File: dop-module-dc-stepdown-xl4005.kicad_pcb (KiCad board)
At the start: 4 copper layers, 53.3 x 27.9 mm, 16 parts, among them J101 Conn_01x02, J102 Conn_01x02, U101 XL4005

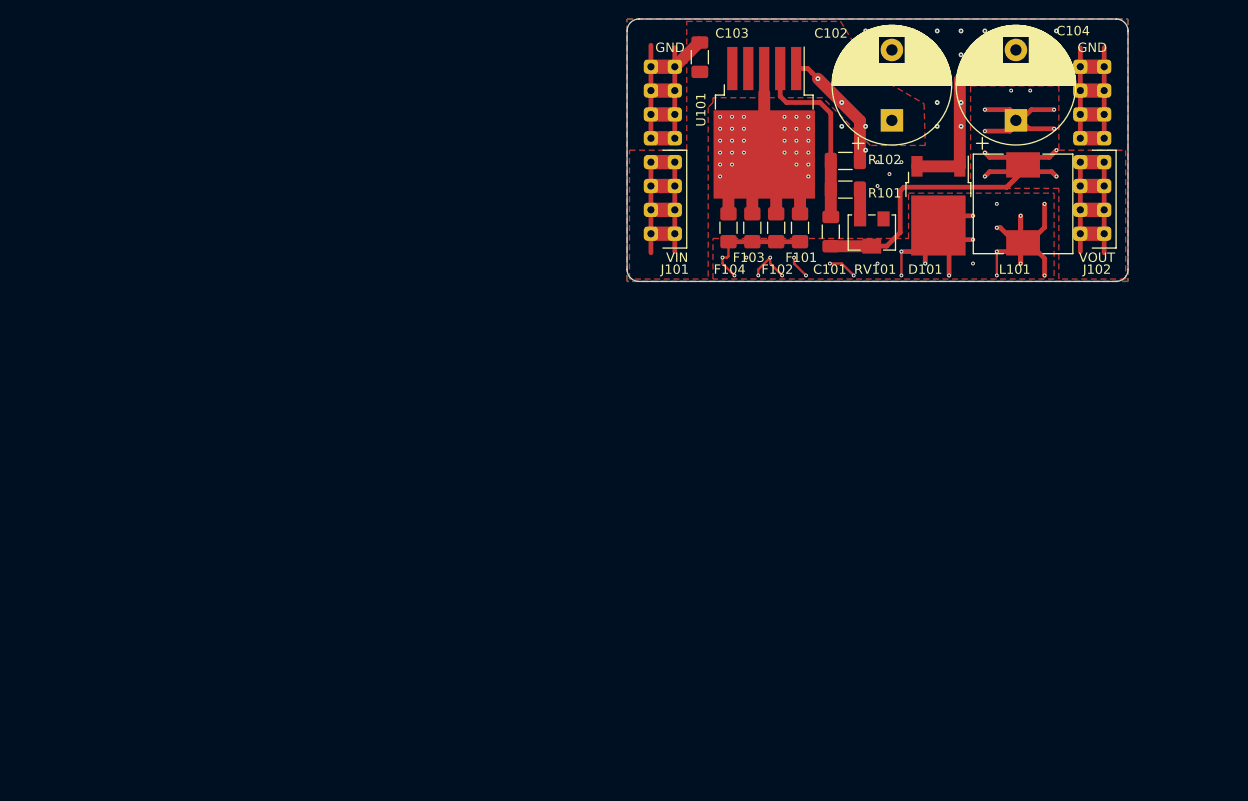
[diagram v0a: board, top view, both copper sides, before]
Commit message: full redesign of the pcb
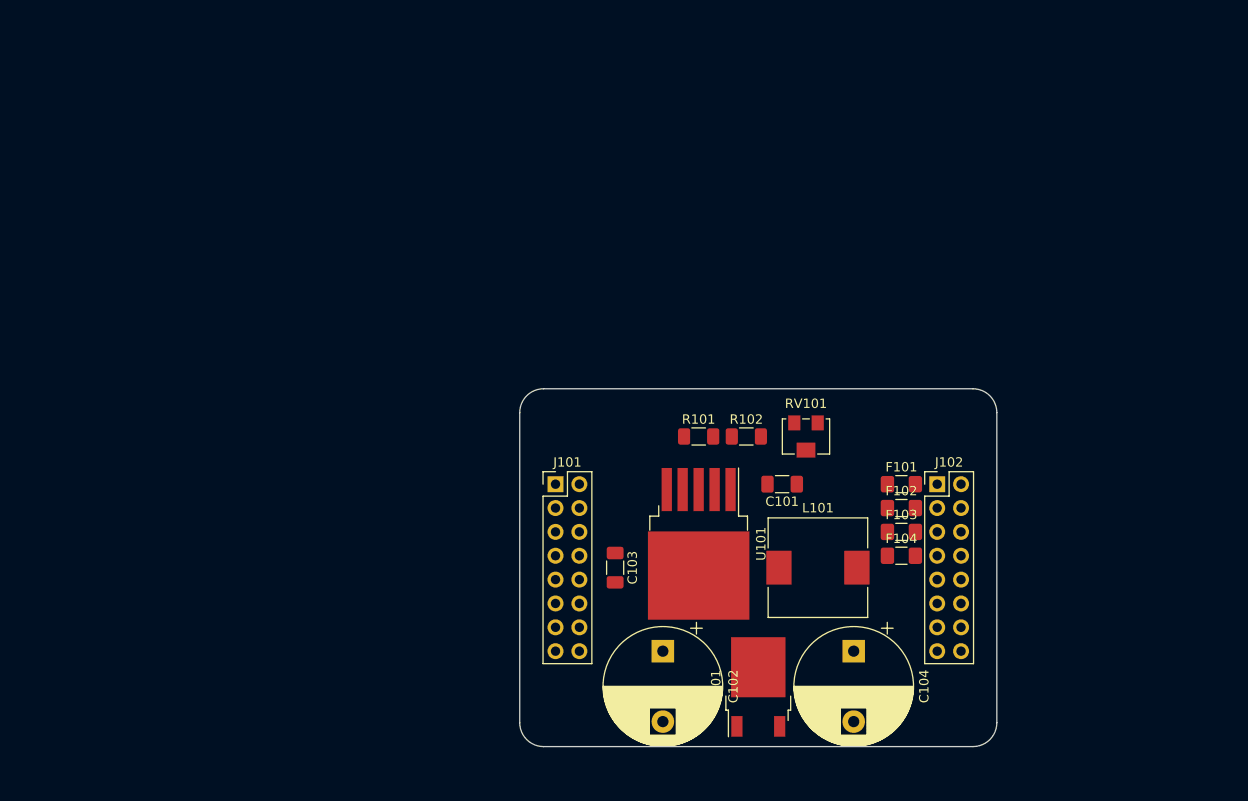
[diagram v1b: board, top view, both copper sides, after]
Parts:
- J101: value Conn_01x02 -> Input; footprint castellated:castellated_2x4_fingers -> Connector_PinHeader_2.54mm:PinHeader_2x08_P2.54mm_Vertical
- J102: value Conn_01x02 -> Output; footprint castellated:castellated_2x4_fingers -> Connector_PinHeader_2.54mm:PinHeader_2x08_P2.54mm_Vertical
- moved C102 61.6 mm to (91.4, 180.3), turned to 270 degrees
- moved C104 59.1 mm to (111.8, 180.3), turned to 270 degrees
- moved C103 55.1 mm to (86.4, 171.4), turned to 270 degrees
- moved D101 54.7 mm to (101.6, 184.2), turned to 90 degrees
- moved U101 45.4 mm to (95.2, 168.9)
- moved L101 44.5 mm to (108.0, 171.4), turned to 0 degrees
- moved F104 39.5 mm to (116.8, 170.2), turned to 0 degrees
- moved J102 39.2 mm to (120.7, 162.6), turned to 0 degrees
- moved J101 37.4 mm to (80.0, 162.6), turned to 0 degrees
- moved F103 36.1 mm to (116.8, 167.6), turned to 0 degrees
- moved F102 32.7 mm to (116.8, 165.1), turned to 0 degrees
- moved R102 31.2 mm to (100.3, 157.5)
- moved R101 30.6 mm to (95.2, 157.5), turned to 0 degrees
- moved F101 29.4 mm to (116.8, 162.6), turned to 0 degrees
- moved C101 27.4 mm to (104.1, 162.6), turned to 180 degrees
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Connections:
- F101 pad 1: Net-(D101-Pad2) -> Net-(F101-Pad1)
- F101 pad 2: Net-(F101-Pad2) -> +5V
- F102 pad 1: Net-(D101-Pad2) -> Net-(F101-Pad1)
- F102 pad 2: Net-(F101-Pad2) -> +5V
- F103 pad 1: Net-(D101-Pad2) -> Net-(F101-Pad1)
- F103 pad 2: Net-(F101-Pad2) -> +5V
- F104 pad 1: Net-(D101-Pad2) -> Net-(F101-Pad1)
- F104 pad 2: Net-(F101-Pad2) -> +5V
- J101 pad 2: GND -> +15V
- J102 pad 1: +5V -> Net-(F101-Pad1)
- J102 pad 2: GND -> Net-(F101-Pad1)
- U101 pad 3: Net-(F101-Pad2) -> Net-(D101-Pad2)
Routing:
- net +5V: track 95.0 -> 0.00 mm, vias 10 -> 0
- net GND: track 91.5 -> 0.00 mm, vias 33 -> 0
- net Net-(D101-Pad2): track 85.1 -> 0.00 mm, vias 26 -> 0
- net Net-(F101-Pad2): track 38.6 -> 0.00 mm, vias 30 -> 0
- net +15V: track 29.3 -> 0.00 mm
- net Net-(C101-Pad2): track 20.1 -> 0.00 mm
- net Net-(R101-Pad1): track 3.13 -> 0.00 mm
- removed copper zone on F.Cu, net +15V
- removed copper zone on In2.Cu, net +15V
- removed copper zone on F.Cu, net +5V
- removed copper zone on In2.Cu, net +5V
- removed copper zone on F.Cu, net GND
- removed copper zone on F.Cu, net Net-(D101-Pad2)
- removed copper zone on In2.Cu, net Net-(D101-Pad2)
- removed copper zone on B.Cu, net Net-(F101-Pad2)
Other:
- board size 53.3 x 27.9 mm -> 50.8 x 38.1 mm
- board text removed: "5V 12V"
- board text removed: "CC-0 DC stepdown xl4005 module"
- board text removed: "GND"
- board text removed: "GND VIN"
- board text removed: "GND VOUT"
- board text removed: "JLCJLCJLCJLC"
- board text removed: "Up to 4A or 20W max WITHOUT WARRANTY of any kind !"
- board text removed: "VIN"
- board text removed: "VOUT"

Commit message: complete rework
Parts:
- removed F101, F102, F103, F104: 1A, Fuse:Fuse_1206_3216Metric_Pad1.42x1.75mm_HandSolder
- added G***: LOGO, cliparts:logo--cc--zero, F.Cu at (95.9, 177.8)
- added G***: LOGO, cliparts:logo--cc--cc, F.Cu at (91.4, 177.8)
- added J103: V_OUT, Connector_PinHeader_2.54mm:PinHeader_1x04_P2.54mm_Vertical, F.Cu at (101.0, 158.8)
- added J104: GND_OUT, Connector_PinHeader_2.54mm:PinHeader_1x04_P2.54mm_Vertical, F.Cu at (101.0, 183.5)
- C102, C104: footprint Capacitor_THT:CP_Radial_D12.5mm_P7.50mm -> Capacitor_THT:CP_Radial_D13.0mm_P5.00mm
- J101: value Input -> V_IN; footprint Connector_PinHeader_2.54mm:PinHeader_2x08_P2.54mm_Vertical -> Connector_PinHeader_2.54mm:PinHeader_2x02_P2.54mm_Vertical
- J102: value Output -> GND_IN; footprint Connector_PinHeader_2.54mm:PinHeader_2x08_P2.54mm_Vertical -> Connector_PinHeader_2.54mm:PinHeader_2x02_P2.54mm_Vertical
- L101: footprint Inductor_SMD:L_10.4x10.4_H4.8 -> coilcraft_THT:CoilCraft_AGP2923
- moved J102 88.3 mm to (34.3, 181.0)
- moved RV101 50.3 mm to (56.5, 161.3)
- moved C102 47.8 mm to (44.5, 171.4), turned to 180 degrees
- moved J101 45.9 mm to (34.3, 158.8)
- moved C101 42.5 mm to (61.6, 162.6), turned to 0 degrees
- moved U101 40.8 mm to (55.2, 177.2)
- moved R101 39.7 mm to (56.5, 166.4)
- moved R102 39.7 mm to (61.6, 166.4)
- moved C103 35.9 mm to (50.8, 166.4), turned to 180 degrees
- moved D101 35.8 mm to (66.0, 179.7)
- moved L101 29.2 mm to (78.7, 171.4), turned to 90 degrees
- moved C104 22.0 mm to (95.2, 165.7)
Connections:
- J102 pad 1: Net-(F101-Pad1) -> GND
- J102 pad 2: Net-(F101-Pad1) -> GND
- J102 pad 3: Net-(F101-Pad1) -> GND
- J102 pad 4: Net-(F101-Pad1) -> GND
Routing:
- net Net-(D101-Pad2): track 0.00 -> 33.6 mm, vias 0 -> 16
- net +5V: track 0.00 -> 16.4 mm
- net Net-(C101-Pad2): track 0.00 -> 12.6 mm
- net GND: track 0.00 -> 11.3 mm, vias 0 -> 4
- net +15V: track 0.00 -> 10.7 mm
- net Net-(R101-Pad1): track 0.00 -> 7.47 mm
- added copper zone on F.Cu, net +15V
- added copper zone on F.Cu, net +5V
- added copper zone on B.Cu, net GND
- added copper zone on F.Cu, net GND
- added copper zone on F.Cu, net Net-(D101-Pad2)
- removed copper zone on In1.Cu, net GND
- removed copper zone on In2.Cu, net GND
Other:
- board size 50.8 x 38.1 mm -> 76.8 x 34.9 mm

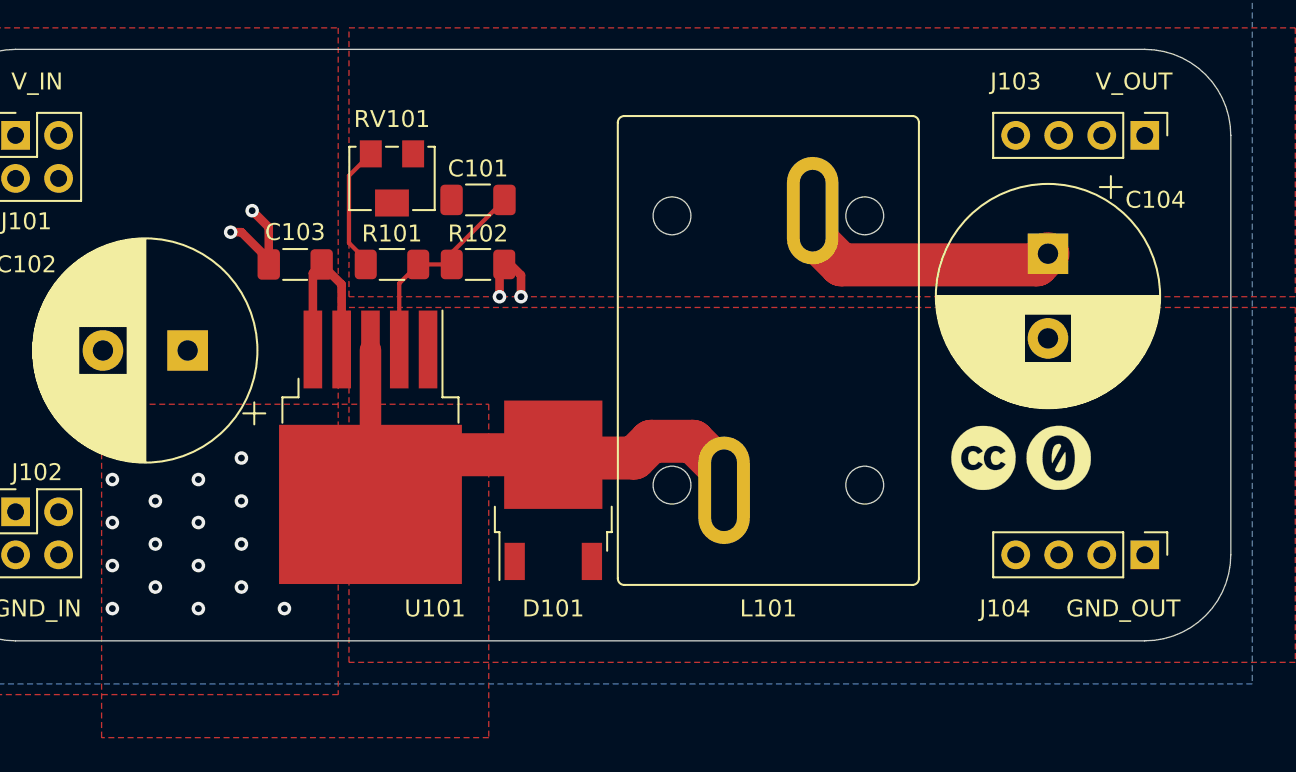
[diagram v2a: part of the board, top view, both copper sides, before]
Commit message: add copper pour for heat dissipation on the bottom, fixes DRC violations
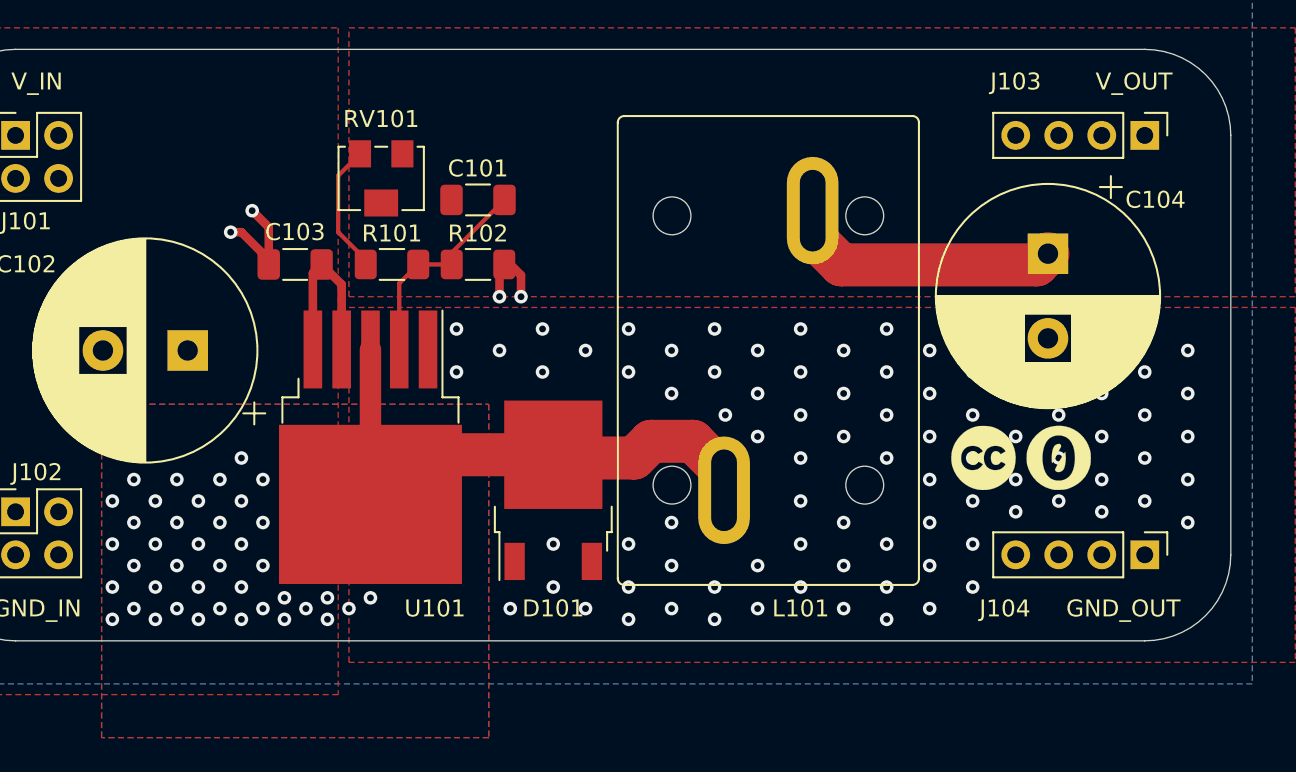
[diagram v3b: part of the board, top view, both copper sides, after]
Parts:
- moved RV101 0.63 mm to (55.9, 161.3)
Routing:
- net Net-(D101-Pad2): vias 16 -> 40
- net GND: vias 4 -> 90
- added copper zone on B.Cu, net Net-(D101-Pad2)
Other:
- copper layers 4 -> 2

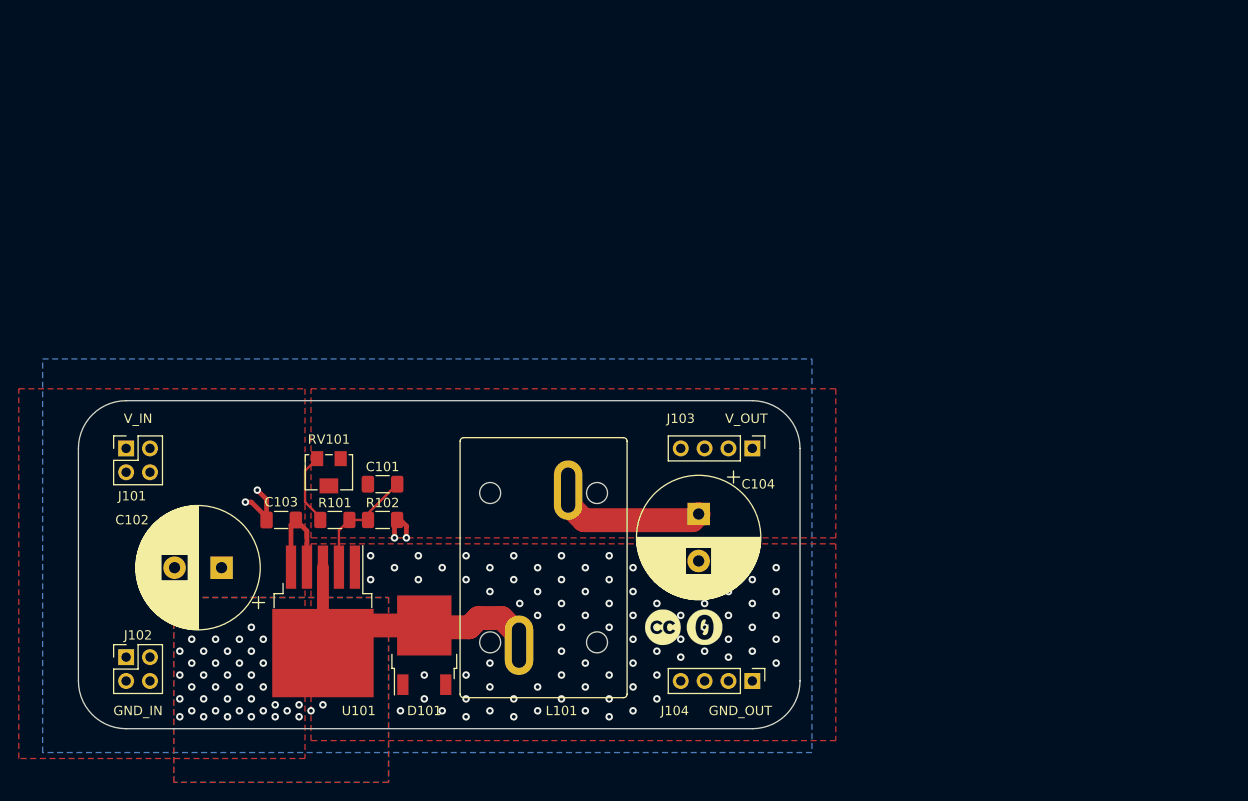
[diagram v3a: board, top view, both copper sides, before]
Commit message: update cartridge, center pcb in worksheet, use new page description
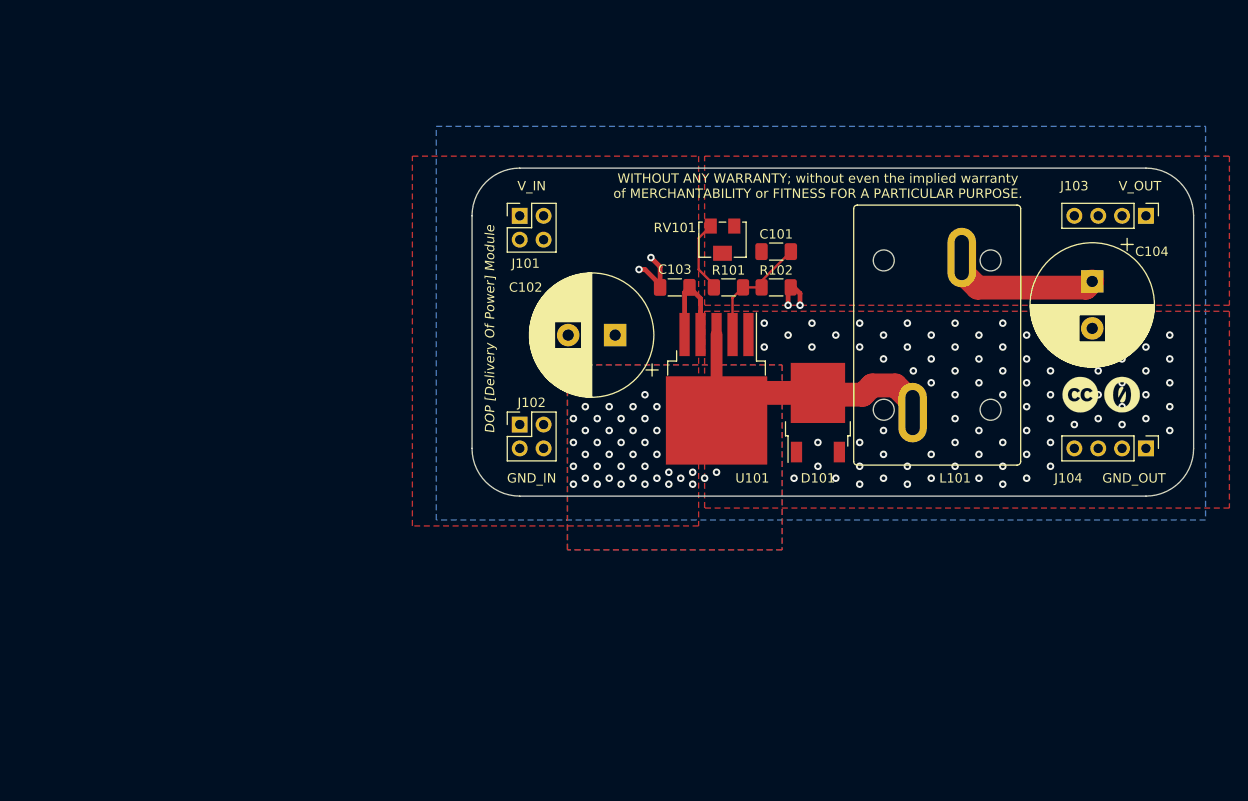
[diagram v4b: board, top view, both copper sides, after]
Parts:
- moved G*** 50.9 mm to (140.3, 153.0)
- moved G*** 50.9 mm to (135.9, 153.0)
- moved C101 48.7 mm to (103.5, 137.8)
- moved C103 48.7 mm to (92.7, 141.6)
- moved C104 48.7 mm to (137.2, 141.0)
- moved D101 48.7 mm to (108.0, 154.9)
- moved R101 48.7 mm to (98.4, 141.6)
- moved R102 48.7 mm to (103.5, 141.6)
- moved L101 48.7 mm to (120.7, 146.7)
- moved J101 48.7 mm to (76.2, 134.0)
- moved J102 48.7 mm to (76.2, 156.2)
- moved RV101 48.7 mm to (97.8, 136.5)
- moved U101 48.7 mm to (97.2, 152.4)
- moved C102 48.7 mm to (86.4, 146.7)
- moved J103 48.7 mm to (142.9, 134.0)
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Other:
- board text added: "DOP [Delivery Of Power] Module"
- board text added: "WITHOUT ANY WARRANTY; without even the implied warranty of MERCHANTABILITY or FITNESS FOR A PARTICULAR PURPOSE."
